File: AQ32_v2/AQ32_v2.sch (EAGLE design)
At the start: 113 parts, among them Q2 BCV27, Q3 BCV27, Q5 BCV27, Q6 BCV27, U1 ITG-3200, U10 MS5611, U11 MIC5239, U13 74AHC1G86DCK, U2 STM32F10XVXT6, U7 USD-SOCKETNEW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

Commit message: completed connections to external JST connectors
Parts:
- removed X3, X4, X5, X6: SM04B-SRSS-TB, con-jst2:SM04B-SRSS-TB
- removed X7: SM06B-SRSS-TB, con-jst2:SM06B-SRSS-TB
- removed X8: BM04B-SRSS-TB, con-jst2:BM04B-SRSS-TB
- added I2C, SERIAL: SM04B-SRSS-TB, con-jst2:SM04B-SRSS-TB
- added OSD: SM07B-SRSS-TB, con-jst2:SM07B-SRSS-TB
- JP3-1, JP3-2: value (none) -> M09LOCK; device SparkFun-Connectors:M08LOCK -> SparkFun-Connectors:M09LOCK
- renumbered X9 to GPS
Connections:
- net OUT3 renamed LEDGND3
- removed net N$16: JP1-1.6
- removed net N$17: JP1-1.7
- removed net N$4: JP2-3.9
- removed net OUT1: JP3-2.1, Q5.C
- removed net OUT2: JP3-2.2, Q2.C
- removed net OUT4: JP3-2.4, Q6.C
- new net LEDGND1: JP3-2.2, Q5.C
- new net LEDGND2: JP3-1.2, Q2.C
- new net LEDGND4: JP3-1.3, Q6.C
- new net NSS_LV/DAC_OUT1: JP3-2.9
- net 3V3AN: now also I2C-1.S, JP3-2.7, SERIAL-1.S
- net 5V-3: now also OSD-1.S, OSD-6.S
- net 5V-4: now also JP3-2.8
- net ADC123_IN12: now also JP3-1.4
- net ADC123_IN13: now also JP1-2.6
- net ADC12_IN14: now also JP3-1.7
- net ADC12_IN15: now also JP3-1.5
- net GND: now also I2C-4.S, JP1-1.6, JP1-1.7, JP3-1.8, JP3-1.9, OSD-7.S, SERIAL-4.S; no longer JP1-2.7, JP3-1.1, JP3-1.2, JP3-1.3, JP3-1.4
- net JTAG-TRST: now also JP3-2.6
- net JTCK: now also JP3-2.5
- net JTMS: now also JP3-2.4
- net LIPO: now also JP1-2.7; no longer JP1-2.6
- net MISO2_LV: now also OSD-5.S
- net MOSI2_LV: now also OSD-3.S
- net SCK2_LV: now also OSD-4.S
- net SCL2_LV: now also I2C-2.S
- net SDA2_LV: now also I2C-3.S
- net TIM3_CH3: now also JP2-3.9
- net TIM3_CH4: now also JP3-1.6
- net TIM5_CH4: now also OSD-2.S
- net UART1_RX: now also SERIAL-3.S
- net UART1_TX: now also SERIAL-2.S
- net UART3_RX: now also JP3-2.1
- net UART3_TX: now also JP3-1.1
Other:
- note added: "+5V"
- note added: "3.3V"
- note added: "AI1 (Range Finder)"
- note added: "AI2"
- note added: "AI3"
- note added: "AI4"
- note added: "AI5"
- note added: "CS"
- note added: "DIN"
- note added: "DOUT"
- note added: "GND"
- note added: "RESET"
- note added: "SCK"
- moved on the sheet: JP1-1, JP1-2, JP2-1, JP2-2, JP2-3, R14, R15, R16, R17, R18, R19, R20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

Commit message: move LEDs to separate connector, connected baro to SPI
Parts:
- removed L61: (no value), rcl:R-US_R0805
- added JP4-1, JP4-2: (no value), SparkFun-Connectors:M02LOCK
- added JP5: M01PTH, SparkFun-Connectors:M01PTH
- added L2: 22uH, SparkFun:INDUCTOR0805
- added R39: 10K, SparkFun:RESISTOR0402
- C1: value 10uF -> 4.7uF
- D2, D3: value (none) -> 30V
- JP3-1, JP3-2: value M09LOCK -> M09; device SparkFun-Connectors:M09LOCK -> SparkFun-Connectors:M09
- R11, R4, R57, R6: value 294R -> 330
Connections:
- removed net NSS_LV/DAC_OUT1: JP3-2.9
- removed net PD10: U2PORTD_H.PD10
- removed net PE7: U2PORTE_L.PE7
- new net BARO_CS: R39.1, U10.CSB, U10.CSB@2, U2PORTD_H.PD10
- new net BARO_PS: U10.PS, U2PORTE_L.PE7
- net 3V3AN: no longer JP3-2.7
- net 3V3DIG: now also L2.1, R39.2; no longer L61.1, U10.CSB, U10.CSB@2, U10.PS
- net 5V-2: now also JP2-2.10, JP2-2.11, JP2-2.12; no longer JP2-2.9
- net 5V-3: now also JP2-2.9; no longer JP2-2.10, JP2-2.11, JP2-2.12
- net 5V-4: no longer JP3-2.8
- net 5VIN: now also JP3-2.1
- net ADC123_IN12: now also JP3-2.8; no longer JP3-1.4
- net ADC12_IN14: now also JP3-2.5; no longer JP3-1.7
- net ADC12_IN15: now also JP3-2.7; no longer JP3-1.5
- net GND: now also JP3-1.1, JP3-1.4, JP3-1.5, JP3-1.6, JP3-1.7
- net GPSBATT: now also JP5.1
- net JTAG-TRST: now also JP3-1.3; no longer JP3-2.6
- net JTCK: now also JP3-2.4; no longer JP3-2.5
- net JTMS: now also JP3-2.3; no longer JP3-2.4
- net LEDGND1: now also JP4-1.1; no longer JP3-2.2
- net LEDGND2: now also JP4-1.2; no longer JP3-1.2
- net LEDGND3: now also JP4-2.1; no longer JP3-2.3
- net LEDGND4: now also JP4-2.2; no longer JP3-1.3
- net N$40: now also L2.2; no longer L61.2
- net NSS1_LV/DAC_OUT1: now also JP3-2.9
- net TIM3_CH4: now also JP3-2.6; no longer JP3-1.6
- net UART3_RX: now also JP3-2.2; no longer JP3-2.1
- net UART3_TX: now also JP3-1.2; no longer JP3-1.1
- net UART4_RX: now also U10.SDO
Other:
- note removed: "Inductor!"
- moved on the sheet: C1, C17, C43, C7, JP3-2

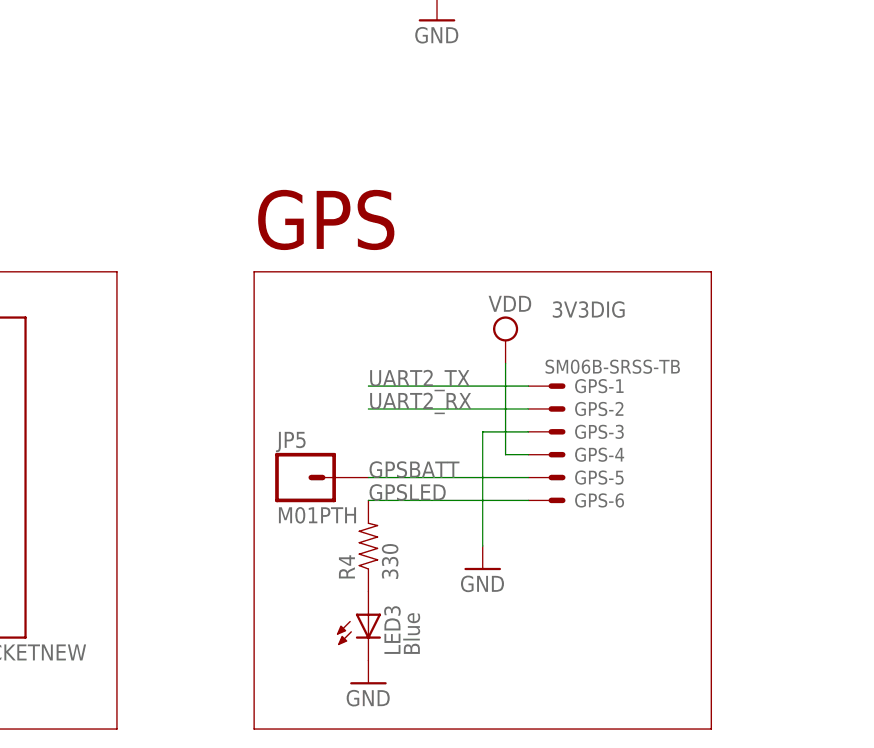
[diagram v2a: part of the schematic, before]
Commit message: added ground pin for GPS battery
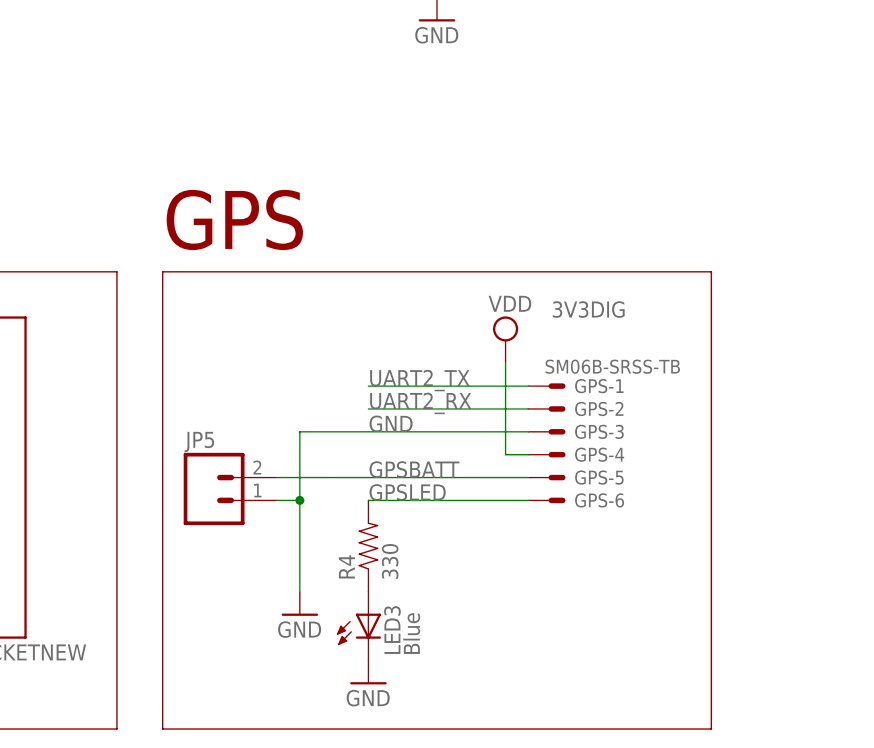
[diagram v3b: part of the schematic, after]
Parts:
- JP5: value M01PTH -> (none); device SparkFun-Connectors:M01PTH -> SparkFun-Connectors:M02PTH
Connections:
- net GND: now also JP5.1
- net GPSBATT: now also JP5.2; no longer JP5.1
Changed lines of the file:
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@@
 <part name="JP3-2" library="SparkFun-Connectors" deviceset="M09" device=""/>
 <part name="R39" library="SparkFun" deviceset="RESISTOR" device="0402" value="10K"/>
-<part name="JP5" library="SparkFun-Connectors" deviceset="M01" device="PTH"/>
+<part name="JP5" library="SparkFun-Connectors" deviceset="M02" device="PTH"/>
 </parts>
 <sheets>
@@
 <text x="256.54" y="190.5" size="6.4516" layer="94">Sensors</text>
 <text x="0" y="-15.24" size="6.4516" layer="94">uSD</text>
-<wire x1="119.38" y1="-17.78" x2="119.38" y2="-68.58" width="0.1524" layer="94"/>
-<wire x1="119.38" y1="-68.58" x2="170.18" y2="-68.58" width="0.1524" layer="94"/>
+<wire x1="109.22" y1="-17.78" x2="109.22" y2="-68.58" width="0.1524" layer="94"/>
+<wire x1="109.22" y1="-68.58" x2="170.18" y2="-68.58" width="0.1524" layer="94"/>
 <wire x1="170.18" y1="-68.58" x2="170.18" y2="-17.78" width="0.1524" layer="94"/>
-<wire x1="170.18" y1="-17.78" x2="119.38" y2="-17.78" width="0.1524" layer="94"/>
-<text x="119.38" y="-15.24" size="6.4516" layer="94">GPS</text>
+<wire x1="170.18" y1="-17.78" x2="109.22" y2="-17.78" width="0.1524" layer="94"/>
+<text x="109.22" y="-15.24" size="6.4516" layer="94">GPS</text>
 <wire x1="398.78" y1="116.84" x2="436.88" y2="116.84" width="0.1524" layer="94"/>
 <wire x1="436.88" y1="116.84" x2="436.88" y2="91.44" width="0.1524" layer="94"/>
@@
 <instance part="GND12" gate="1" x="342.9" y="134.62"/>
 <instance part="R53" gate="G$1" x="40.64" y="-27.94"/>
-<instance part="GND16" gate="1" x="144.78" y="-50.8"/>
+<instance part="GND16" gate="1" x="124.46" y="-55.88"/>
 <instance part="SUPPLY7" gate="G$1" x="147.32" y="-25.4"/>
 <instance part="GND47" gate="1" x="22.86" y="5.08"/>
@@
 <instance part="JP3-2" gate="G$1" x="472.44" y="68.58"/>
 <instance part="R39" gate="G$1" x="279.4" y="50.8" rot="R90"/>
-<instance part="JP5" gate="G$1" x="124.46" y="-40.64"/>
+<instance part="JP5" gate="G$1" x="114.3" y="-43.18"/>
 </instances>
 <busses>
@@
 </segment>
 <segment>
-<wire x1="144.78" y1="-48.26" x2="144.78" y2="-35.56" width="0.1524" layer="91"/>
-<wire x1="144.78" y1="-35.56" x2="149.86" y2="-35.56" width="0.1524" layer="91"/>
+<wire x1="124.46" y1="-53.34" x2="124.46" y2="-43.18" width="0.1524" layer="91"/>
+<wire x1="124.46" y1="-43.18" x2="124.46" y2="-35.56" width="0.1524" layer="91"/>
+<wire x1="124.46" y1="-35.56" x2="149.86" y2="-35.56" width="0.1524" layer="91"/>
 <pinref part="GND16" gate="1" pin="GND"/>
 <pinref part="GPS" gate="-3" pin="S"/>
+<pinref part="JP5" gate="G$1" pin="1"/>
+<wire x1="121.92" y1="-43.18" x2="124.46" y2="-43.18" width="0.1524" layer="91"/>
+<junction x="124.46" y="-43.18"/>
+<label x="132.08" y="-35.56" size="1.778" layer="95"/>
 </segment>
 <segment>
@@
 <net name="GPSBATT" class="0">
 <segment>
-<wire x1="149.86" y1="-40.64" x2="132.08" y2="-40.64" width="0.1524" layer="91"/>
+<wire x1="149.86" y1="-40.64" x2="127" y2="-40.64" width="0.1524" layer="91"/>
 <label x="132.08" y="-40.64" size="1.778" layer="95"/>
 <pinref part="GPS" gate="-5" pin="S"/>
-<pinref part="JP5" gate="G$1" pin="1"/>
-</segment>
-</net>
+<pinref part="JP5" gate="G$1" pin="2"/>
+<wire x1="121.92" y1="-40.64" x2="127" y2="-40.64" width="0.1524" layer="91"/>
+</segment>
+</net>
